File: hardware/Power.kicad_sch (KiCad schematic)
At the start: 42 parts, among them Q1 Q_NMOS, Q2 Q_NMOS, Q3 Q_NMOS, Q4 Q_NMOS, Q5 Q_PMOS, U5 BQ25798RQMR

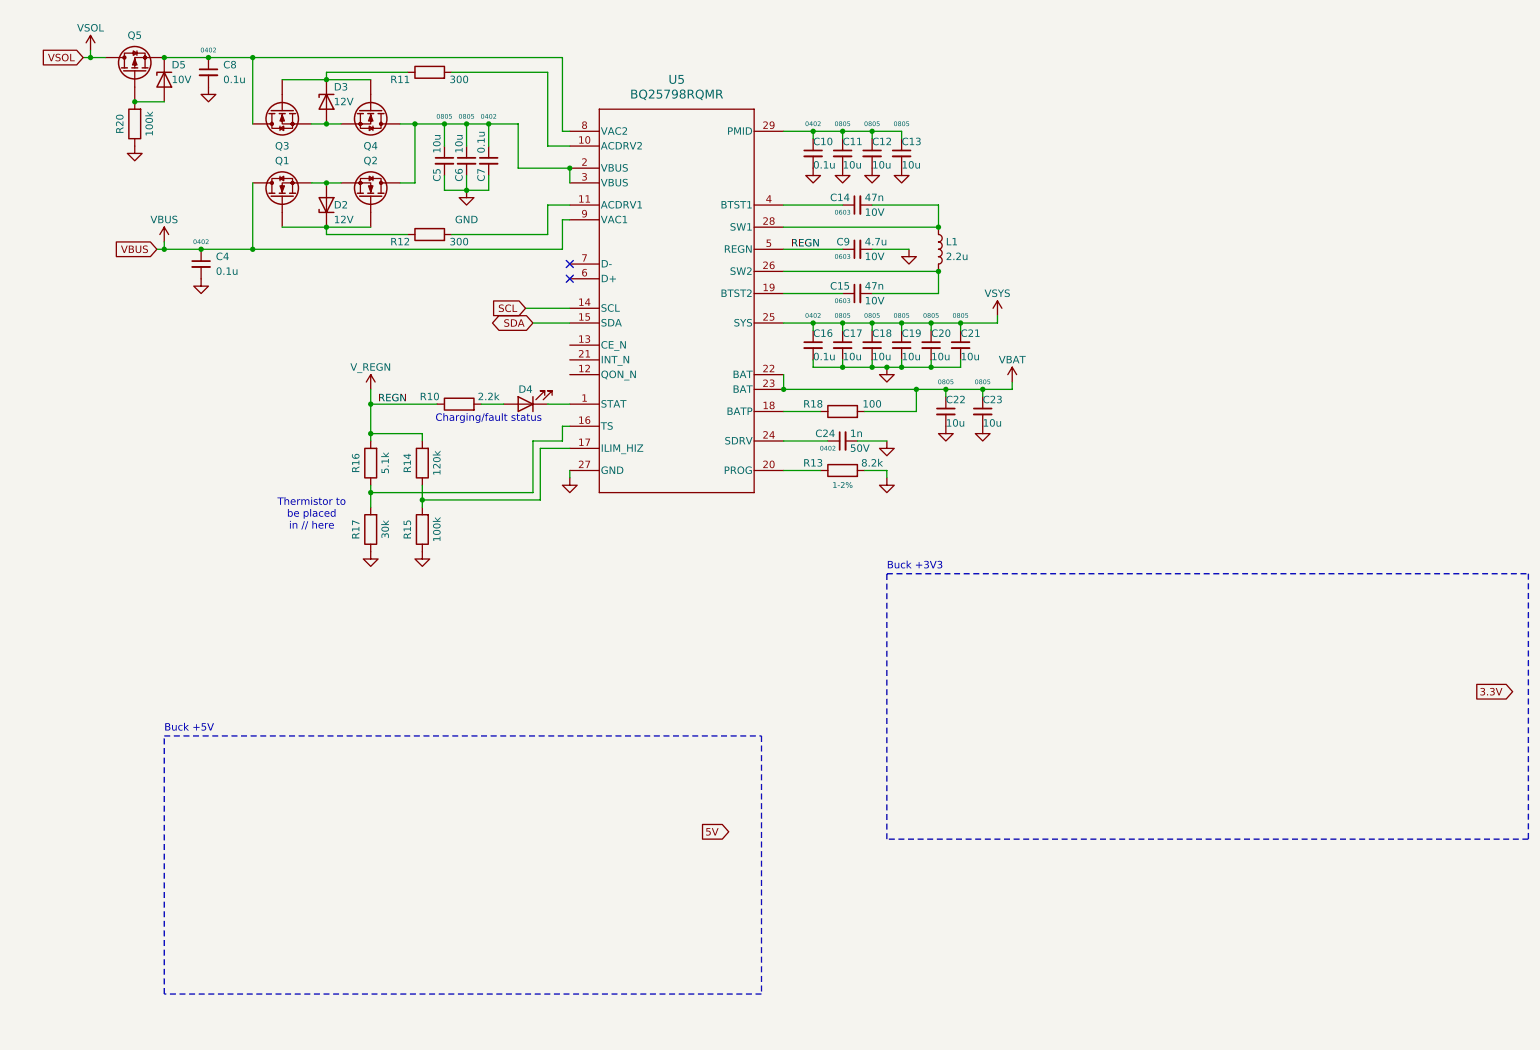
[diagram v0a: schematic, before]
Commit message: Add BQ25798 debug pins to ESP and placed TP & headers
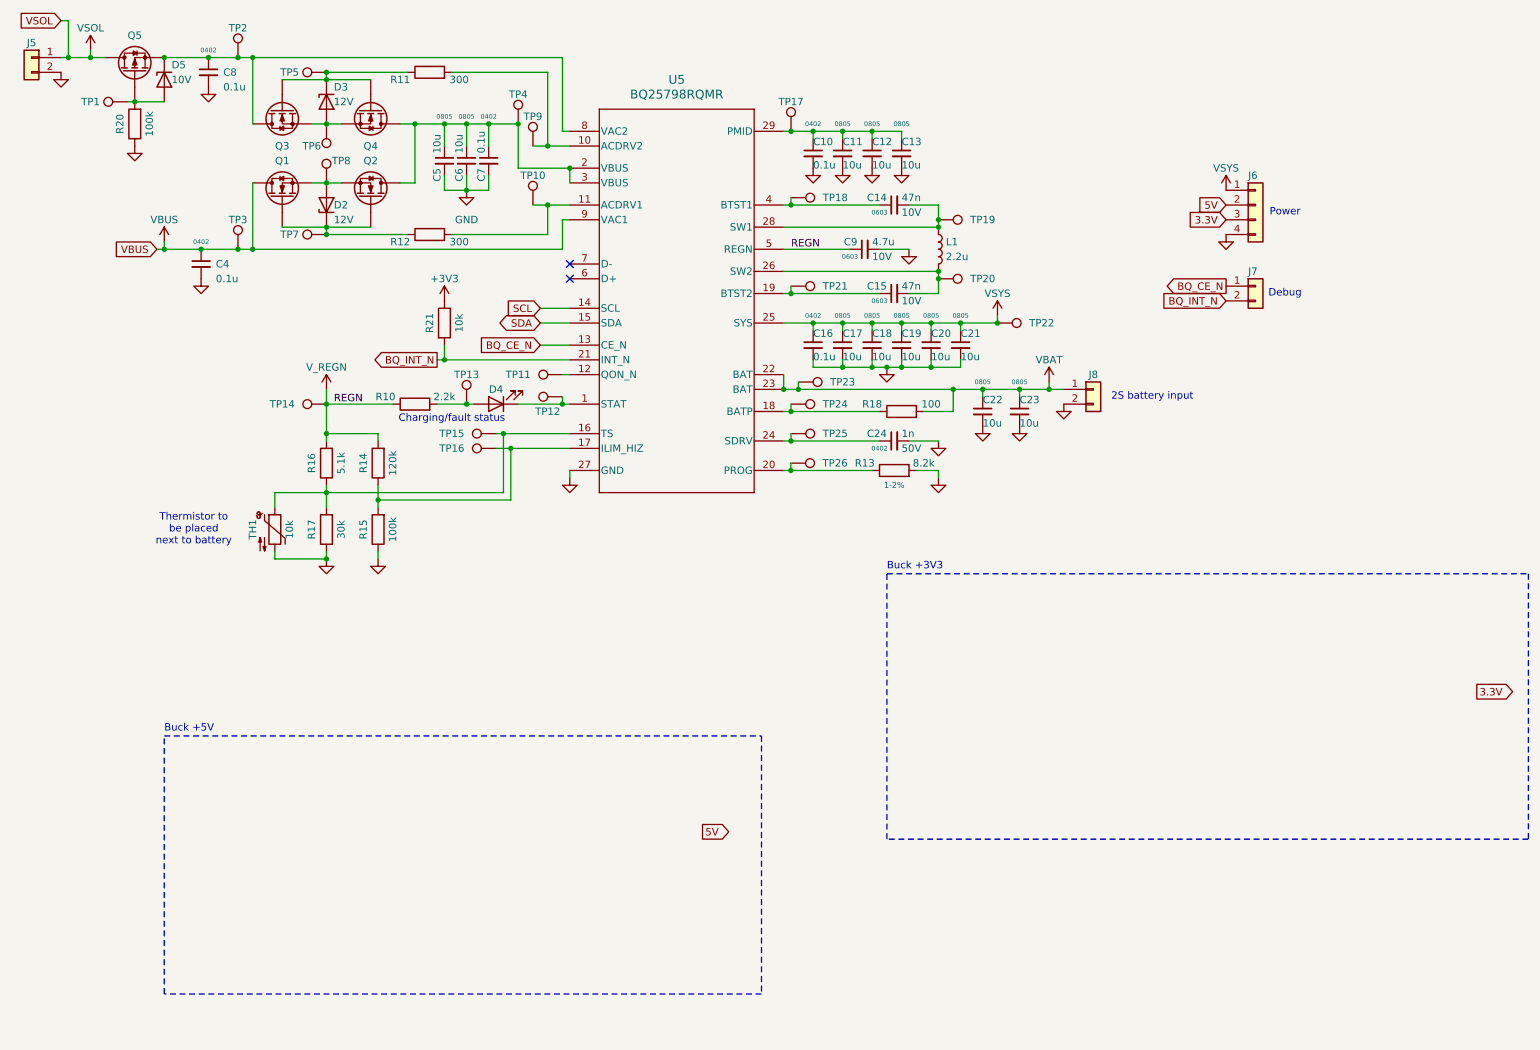
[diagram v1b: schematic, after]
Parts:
- added J5, J7, J8: Conn_01x02, symbol Connector_Generic:Conn_01x02
- added J6: Conn_01x04, symbol Connector_Generic:Conn_01x04
- added R21: 10k, Resistor_SMD:R_0402_1005Metric, symbol Device:R
- added TH1: 10k, symbol Device:Thermistor_NTC
- added TP1, TP10, TP11, TP12, TP13, TP14, TP15, TP16, TP17, TP18, TP19, TP2, TP20, TP21, TP22, TP23, TP24, TP25, TP26, TP3, TP4, TP5, TP6, TP7, TP8, TP9: TestPoint, symbol Connector:TestPoint
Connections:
- net 3.3V: now also J6.3 (Pin_3)
- net 5V: now also J6.2 (Pin_2)
- net GND: now also J5.2 (Pin_2), J6.4 (Pin_4), J8.2 (Pin_2), TH1.2
- net VBAT: now also J8.1 (Pin_1), TP23.1
- net VBUS: now also TP3.1
- net VSOL: now also J5.1 (Pin_1)
- net VSYS: now also J6.1 (Pin_1), TP22.1
- net V_REGN: now also TP14.1
- net at C10.1, C11.1, C12.1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: now also TP17.1
- net at R18.1, U5.18 (BATP): now also TP24.1
- net at C5.1, C6.1, C7.1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: now also TP4.1
- net at D5.2 (A), Q5.G, R20.2: now also TP1.1
- net at C8.1, D5.1 (K), Q3.D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: now also TP2.1
- net at C15.1, U5.19 (BTST2): now also TP21.1
- net at C15.2, L1.2, U5.26 (SW2): now also TP20.1
- net at D3.1 (K), Q3.G, Q4.G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: now also TP5.1
- net at D3.2 (A), Q3.S, Q4.S: now also TP6.1
- net at D2.1 (K), Q1.G, Q2.G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: now also TP7.1
- net at D2.2 (A), Q1.S, Q2.S: now also TP8.1
- net at R14.1, R15.2, U5.17 (ILIM_HIZ): now also TP16.1
- net at C24.1, U5.24 (SDRV): now also TP25.1
- net at D4.1 (K), U5.1 (STAT): now also TP12.1
- net at R11.2, U5.10 (ACDRV2): now also TP9.1
- net at R12.2, U5.11 (ACDRV1): now also TP10.1
- net at U5.12 (QON_N): now also TP11.1
- net BQ_CE_N: now reaches U5.13 (CE_N)
- net BQ_CE_N: now also J7.1 (Pin_1)
- net at R16.1, R17.2, U5.16 (TS): now also TH1.1, TP15.1
- net at R13.1, U5.20 (PROG): now also TP26.1
- net BQ_INT_N: now reaches U5.21 (INT_N)
- net BQ_INT_N: now also J7.2 (Pin_2), R21.2
- net at C14.2, L1.1, U5.28 (SW1): now also TP19.1
- net at C14.1, U5.4 (BTST1): now also TP18.1
- net at D4.2 (A), R10.2: now also TP13.1
- new net +3V3: R21.1
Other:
- note added: "2S battery input"
- note added: "Debug"
- note added: "Power"
- note added: "Thermistor to be placed next to battery"
- note removed: "Thermistor to be placed in // here"
- moved on the sheet: C14, C15, C22, C23, C24, C9, D4, R10, R13, R14, R15, R16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

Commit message: Add shunt resistor current sensing to solar input
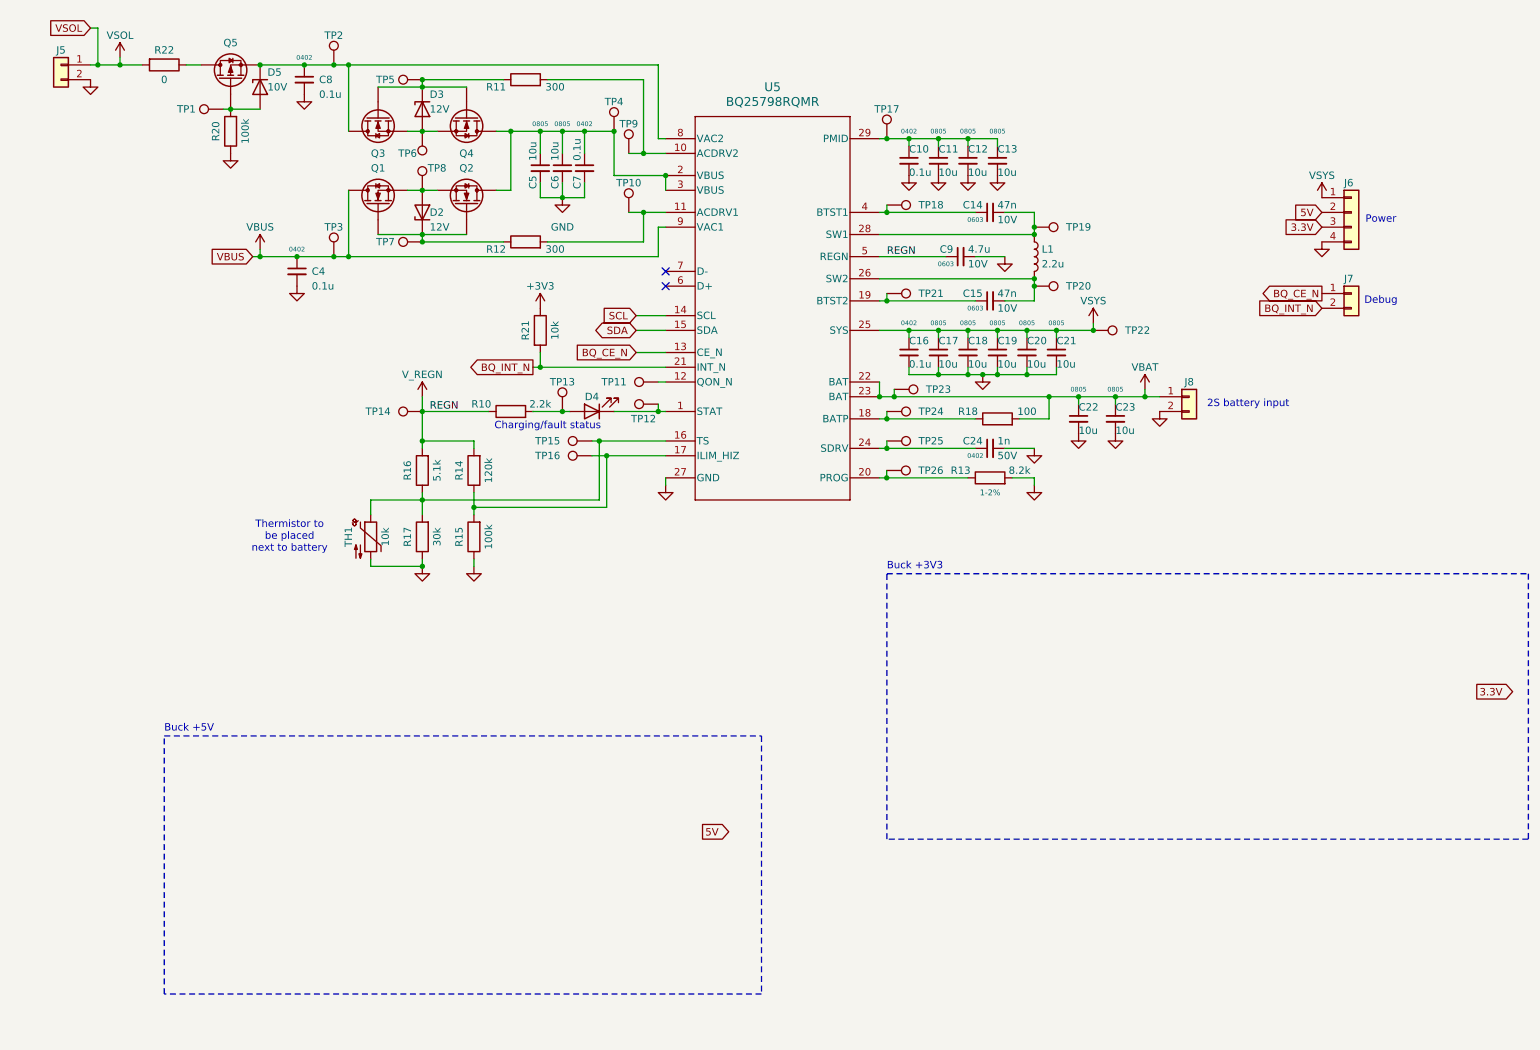
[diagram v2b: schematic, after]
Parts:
- added R22: 0, Resistor_SMD:R_0402_1005Metric, symbol Device:R
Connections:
- net VSOL: now also R22.2; no longer Q5.D
- new net: Q5.D, R22.1
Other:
- moved on the sheet: C10, C11, C12, C13, C14, C15, C16, C17, C18, C19, C20, C21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

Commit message: Added battery NTC thermistor footprint
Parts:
- added R23: 10k, Resistor_SMD:R_0402_1005Metric, symbol Device:R
- TH1: footprint (none) -> GoG_Library:Thermistor NTC
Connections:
- net BQ_CE_N: now also R23.2
- net GND: now also R23.1
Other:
- moved on the sheet: R21
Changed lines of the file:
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@@
 	)
 	(junction
+		(at 114.3 74.93)
+		(diameter 0)
+		(color 0 0 0 0)
+	)
+	(junction
 		(at 182.88 78.74)
 		(diameter 0)
@@
 	(wire
 		(pts
-			(xy 105.41 77.47) (xy 106.68 77.47)
+			(xy 104.14 77.47) (xy 106.68 77.47)
 		)
 		(stroke
@@
 	(wire
 		(pts
-			(xy 106.68 74.93) (xy 106.68 77.47)
+			(xy 106.68 73.66) (xy 106.68 77.47)
 		)
 		(stroke
@@
 	(wire
 		(pts
-			(xy 123.19 71.12) (xy 128.27 71.12)
+			(xy 125.73 71.12) (xy 128.27 71.12)
 		)
 		(stroke
@@
 	(wire
 		(pts
+			(xy 114.3 73.66) (xy 114.3 74.93)
+		)
+		(stroke
+			(width 0)
+			(type default)
+		)
+	)
+	(wire
+		(pts
 			(xy 165.1 62.23) (xy 191.77 62.23)
 		)
@@
 	(wire
 		(pts
-			(xy 123.19 74.93) (xy 128.27 74.93)
+			(xy 104.14 74.93) (xy 114.3 74.93)
 		)
 		(stroke
@@
 	(wire
 		(pts
-			(xy 123.19 68.58) (xy 128.27 68.58)
+			(xy 125.73 68.58) (xy 128.27 68.58)
 		)
 		(stroke
@@
 	(wire
 		(pts
+			(xy 114.3 74.93) (xy 128.27 74.93)
+		)
+		(stroke
+			(width 0)
+			(type default)
+		)
+	)
+	(wire
+		(pts
 			(xy 110.49 36.83) (xy 110.49 40.64)
 		)
@@
 	(global_label "BQ_INT_N"
 		(shape output)
-		(at 105.41 77.47 180)
+		(at 104.14 77.47 180)
 		(fields_autoplaced yes)
 		(effects
@@
 		)
 		(property "Intersheetrefs" "${INTERSHEET_REFS}"
-			(at 93.6557 77.47 0)
+			(at 92.3857 77.47 0)
 			(effects
 				(font
@@
 	(global_label "BQ_CE_N"
 		(shape input)
-		(at 123.19 74.93 180)
+		(at 104.14 74.93 180)
 		(fields_autoplaced yes)
 		(effects
@@
 		)
 		(property "Intersheetrefs" "${INTERSHEET_REFS}"
-			(at 111.9196 74.93 0)
+			(at 92.8696 74.93 0)
 			(effects
 				(font
@@
 	(global_label "SCL"
 		(shape input)
-		(at 123.19 68.58 180)
+		(at 125.73 68.58 180)
 		(fields_autoplaced yes)
 		(effects
@@
 		)
 		(property "Intersheetrefs" "${INTERSHEET_REFS}"
-			(at 116.6972 68.58 0)
+			(at 119.2372 68.58 0)
 			(effects
 				(font
@@
 	(global_label "SDA"
 		(shape bidirectional)
-		(at 123.19 71.12 180)
+		(at 125.73 71.12 180)
 		(fields_autoplaced yes)
 		(effects
@@
 		)
 		(property "Intersheetrefs" "${INTERSHEET_REFS}"
-			(at 115.5254 71.12 0)
+			(at 118.0654 71.12 0)
 			(effects
 				(font
@@
 					(size 1.27 1.27)
 				)
+				(hide yes)
 			)
 		)
@@
 	)
 	(symbol
+		(lib_id "power:GND")
+		(at 114.3 66.04 180)
+		(unit 1)
+		(exclude_from_sim no)
+		(in_bom yes)
+		(on_board yes)
+		(dnp no)
+		(fields_autoplaced yes)
+		(property "Reference" "#PWR014"
+			(at 114.3 59.69 0)
+			(effects
+				(font
+					(size 1.27 1.27)
+				)
+				(hide yes)
+			)
+		)
+		(property "Value" "GND"
+			(at 114.3 60.96 0)
+			(effects
+				(font
+					(size 1.27 1.27)
+				)
+				(hide yes)
+			)
+		)
+		(property "Footprint" ""
+			(at 114.3 66.04 0)
+			(effects
+				(font
+					(size 1.27 1.27)
+				)
+				(hide yes)
+			)
+		)
+		(property "Datasheet" ""
+			(at 114.3 66.04 0)
+			(effects
+				(font
+					(size 1.27 1.27)
+				)
+				(hide yes)
+			)
+		)
+		(property "Description" "Power symbol creates a global label with name \"GND\" , ground"
+			(at 114.3 66.04 0)
+			(effects
+				(font
+					(size 1.27 1.27)
+				)
+				(hide yes)
+			)
+		)
+		(pin "1"
+		)
+		(instances
+			(project "GOG"
+				(path "/5b969f6e-a36e-432b-8f00-b2d6a515a877/c7197dae-6cdc-4538-9538-27053b29fcd0"
+					(reference "#PWR014")
+					(unit 1)
+				)
+			)
+		)
+	)
+	(symbol
 		(lib_id "Device:R")
 		(at 53.34 36.83 180)
@@
 			)
 		)
-		(property "Footprint" ""
+		(property "Footprint" "GoG_Library:Thermistor NTC"
 			(at 77.47 105.41 0)
 			(effects
@@
 			)
 		)
-		(property "Datasheet" "~"
+		(property "Datasheet" "https://4donline.ihs.com/images/VipMasterIC/IC/VISH/VISH-S-A0020584100/VISH-S-A0021262205-1.pdf?hkey=6D3A4C79FDBF58556ACFDE234799DDF0"
 			(at 77.47 105.41 0)
 			(effects
@@
 			)
 		)
-		(property "Description" "Temperature dependent resistor, negative temperature coefficient"
+		(property "Description" "Vishay NTCLE413E2103F102L NTC Thermistor 10k 3435K"
 			(at 77.47 106.68 0)
 			(effects
@@
 	(symbol
 		(lib_id "Device:R")
-		(at 106.68 71.12 0)
+		(at 106.68 69.85 0)
 		(unit 1)
 		(exclude_from_sim no)
@@
 		(dnp no)
 		(property "Reference" "R21"
-			(at 104.14 71.12 90)
+			(at 104.14 69.85 90)
 			(effects
 				(font
@@
 		)
 		(property "Value" "10k"
-			(at 109.22 71.12 90)
+			(at 109.22 69.85 90)
 			(effects
 				(font
@@
 		)
 		(property "Footprint" "Resistor_SMD:R_0402_1005Metric"
-			(at 104.902 71.12 90)
+			(at 104.902 69.85 90)
 			(effects
 				(font
@@
 		)
 		(property "Datasheet" "~"
-			(at 106.68 71.12 0)
+			(at 106.68 69.85 0)
 			(effects
 				(font
@@
 		)
 		(property "Description" "Resistor E12"
-			(at 106.68 71.12 0)
+			(at 106.68 69.85 0)
 			(effects
 				(font
@@
 	)
 	(symbol
+		(lib_id "Device:R")
+		(at 114.3 69.85 0)
+		(unit 1)
+		(exclude_from_sim no)
+		(in_bom yes)
+		(on_board yes)
+		(dnp no)
+		(property "Reference" "R23"
+			(at 111.76 69.85 90)
+			(effects
+				(font
+					(size 1.27 1.27)
+				)
+			)
+		)
+		(property "Value" "10k"
+			(at 116.84 69.85 90)
+			(effects
+				(font
+					(size 1.27 1.27)
+				)
+			)
+		)
+		(property "Footprint" "Resistor_SMD:R_0402_1005Metric"
+			(at 112.522 69.85 90)
+			(effects
+				(font
+					(size 1.27 1.27)
+				)
+				(hide yes)
+			)
+		)
+		(property "Datasheet" "~"
+			(at 114.3 69.85 0)
+			(effects
+				(font
+					(size 1.27 1.27)
+				)
+				(hide yes)
+			)
+		)
+		(property "Description" "Resistor E12"
+			(at 114.3 69.85 0)
+			(effects
+				(font
+					(size 1.27 1.27)
+				)
+				(hide yes)
+			)
+		)
+		(pin "2"
+		)
+		(pin "1"
+		)
+		(instances
+			(project "GOG"
+				(path "/5b969f6e-a36e-432b-8f00-b2d6a515a877/c7197dae-6cdc-4538-9538-27053b29fcd0"
+					(reference "R23")
+					(unit 1)
+				)
+			)
+		)
+	)
+	(symbol
 		(lib_id "power:GND")
 		(at 182.88 78.74 0)
@@
 	(symbol
 		(lib_id "power:+3V3")
-		(at 106.68 67.31 0)
+		(at 106.68 66.04 0)
 		(unit 1)
 		(exclude_from_sim no)
@@
 		(dnp no)
 		(property "Reference" "#PWR013"
-			(at 106.68 71.12 0)
+			(at 106.68 69.85 0)
 			(effects
 				(font
@@
 		)
 		(property "Value" "+3V3"
-			(at 106.68 63.5 0)
+			(at 106.68 62.23 0)
 			(effects
 				(font
@@
 		)
 		(property "Footprint" ""
-			(at 106.68 67.31 0)
+			(at 106.68 66.04 0)
 			(effects
 				(font
@@
 		)
 		(property "Datasheet" ""
-			(at 106.68 67.31 0)
+			(at 106.68 66.04 0)
 			(effects
 				(font
@@
 		)
 		(property "Description" "Power symbol creates a global label with name \"+3V3\""
-			(at 106.68 67.31 0)
+			(at 106.68 66.04 0)
 			(effects
 				(font
